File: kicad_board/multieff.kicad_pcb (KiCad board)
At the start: 2 copper layers, 120 x 108.8 mm, 86 parts, among them J1 Wha1, K1 HEADER_MALE_5X1, K2 HEADER_MALE_4X1, K3 easyC-SMD, K4 easyC-SMD, K5 HEADER_MALE_1X1, U1 ADS1115, U1 MCP23017_SO, U2 MCP23017_SO

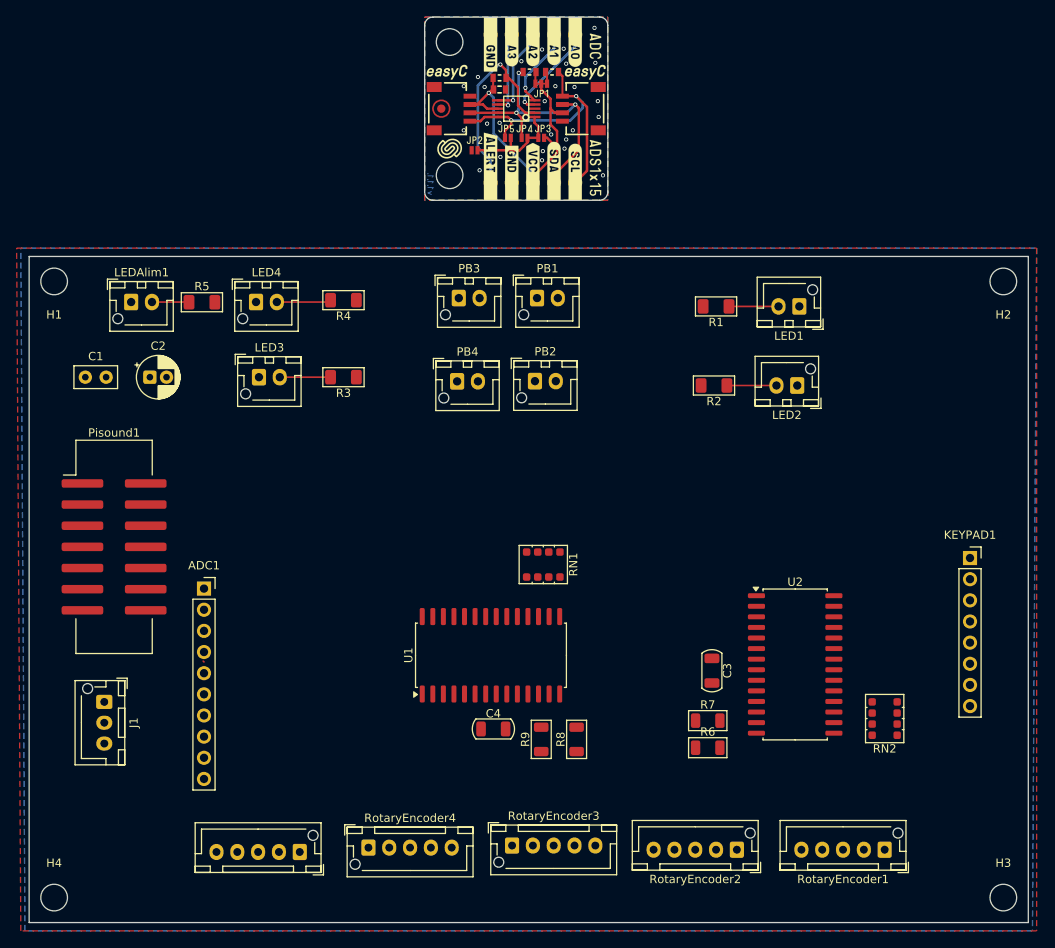
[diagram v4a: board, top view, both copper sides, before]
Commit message: First complete IC based version
Still miss some decoupling condensators.
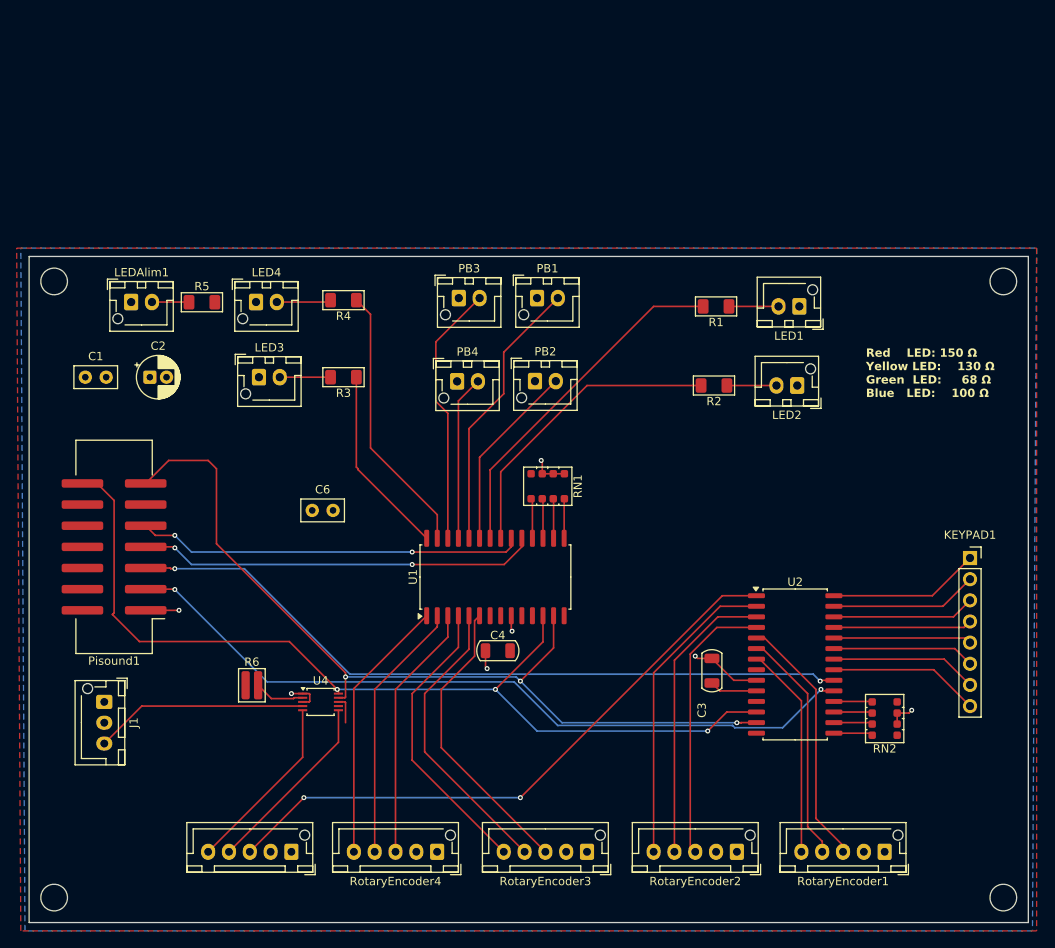
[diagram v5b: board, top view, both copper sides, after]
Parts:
- removed ? (x21): , buzzardLabel
- removed ADC1: Conn_01x10, Connector_PinSocket_2.54mm:PinSocket_1x10_P2.54mm_Vertical
- removed the C1 at (98.5, 11.9)
- removed FD1: FIDUCIAL, e-radionica.com footprinti:FIDUCIAL_23
- removed G***: LOGO, Soldered Graphics:Logo-Back-OSH-3.5mm
- removed G*** (x2): LOGO, Soldered Graphics:Logo-Front-easyC-5mm
- removed G***: LOGO, Soldered Graphics:Logo-Front-Soldered-3mm
- removed G***: LOGO, Soldered Graphics:Symbol-Front-Voltmeter
- removed the H1 at (92.5, 6.25)
- removed the H2 at (92.5, 22.2)
- removed JP1: SMD_JUMPER_3_PAD_TRACE, e-radionica.com footprinti:SMD_JUMPER_3_PAD_TRACE
- removed JP2: 0x48, e-radionica.com footprinti:SMD_JUMPER_CONNECTED
- removed JP3: 0x49, e-radionica.com footprinti:SMD_JUMPER
- removed JP4: 0x4A, e-radionica.com footprinti:SMD_JUMPER
- removed JP5: 0x4B, e-radionica.com footprinti:SMD_JUMPER
- removed K1: HEADER_MALE_5X1, e-radionica.com footprinti:HEADER_MALE_5X1
- removed K2: HEADER_MALE_4X1, e-radionica.com footprinti:HEADER_MALE_4X1
- removed K3, K4: easyC-SMD, e-radionica.com footprinti:easyC-connector
- removed K5: HEADER_MALE_1X1, e-radionica.com footprinti:HEADER_MALE_1X1
- removed the R1 at (98.5, 10.6)
- removed the R2 at (104.8, 9.85)
- removed the R3 at (102.1, 9.85)
- removed R7, R8, R9: 10k, PCM_Resistor_SMD_AKL:R_1206_3216Metric
- removed REF**: Logo-Front-SolderedFULL-13mm, Soldered Graphics:Logo-Back-SolderedFULL-13mm
- removed REF**: Version1.1.1., Soldered Graphics:Version1.1.1.
- removed REF**: Symbol-Front-I2C-ADDR-Field, Soldered Graphics:Symbol-Front-I2C-ADDR-Field
- removed the U1 at (100.5, 14.2)
- added C6: 1uF, Capacitor_THT:C_Disc_D5.0mm_W2.5mm_P2.50mm, F.Cu at (76.0, 62.5)
- added U4: ADS1115IDGS, Package_SO:TSSOP-10_3x3mm_P0.5mm, F.Cu at (77.0, 85.5)
- C3, C4: value 1uF -> 0.1uF
- R1: value 480 -> 150
- R2: value 480 -> 130
- R3: value 480 -> 68
- R4, R5: value 480 -> 100
- R6: footprint PCM_Resistor_SMD_AKL:R_1206_3216Metric -> PCM_Resistor_SMD_AKL:R_0612_1632Metric
- moved R6 55.3 mm to (68.8, 83.5)
- moved C4 9.42 mm to (98.3, 79.3)
- moved U1 9.42 mm to (98.0, 70.5)
- moved RN1 9.42 mm to (104.3, 59.6)
- moved RotaryEncoder3 9.03 mm to (109.0, 103.5), turned to 180 degrees
- moved RotaryEncoder4 8.27 mm to (91.0, 103.5), turned to 180 degrees
- moved Joystick1 1.00 mm to (73.5, 103.5)
- moved RotaryEncoder1 0.25 mm to (144.8, 103.5)
- moved RotaryEncoder2 0.25 mm to (127.0, 103.5)
- turned Pisound1 to 180 degrees
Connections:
- Pisound1 pad 11: unconnected-(Pisound1-Pin_11-Pad11) -> +3.3V
- R1 pad 2: Net-(U1-GPA4) -> Net-(U1-GPA1)
- R2 pad 2: Net-(U1-GPA6) -> Net-(U1-GPA0)
- R3 pad 1: Net-(U1-GPA0) -> Net-(U1-GPA7)
- R4 pad 1: Net-(U1-GPA1) -> Net-(U1-GPA6)
- R6 pad 2: /SDA -> Net-(U4-ALERT/RDY)
- U1 pad 1: Net-(RotaryEncoder4-Pin_3) -> Net-(RotaryEncoder4-Pin_5)
- U1 pad 23: Net-(PB3-Pin_2) -> Net-(PB2-Pin_2)
- U1 pad 24: Net-(PB4-Pin_2) -> Net-(PB1-Pin_2)
- U1 pad 25: Net-(U1-GPA4) -> Net-(PB4-Pin_2)
- U1 pad 26: Net-(PB1-Pin_2) -> Net-(PB3-Pin_2)
- U1 pad 28: Net-(PB2-Pin_2) -> Net-(U1-GPA7)
- U1 pad 3: Net-(RotaryEncoder4-Pin_5) -> Net-(RotaryEncoder4-Pin_3)
- U1 pad 4: Net-(RotaryEncoder3-Pin_3) -> Net-(RotaryEncoder3-Pin_5)
- U1 pad 6: Net-(RotaryEncoder3-Pin_5) -> Net-(RotaryEncoder3-Pin_3)
- U2 pad 5: Net-(RotaryEncoder1-Pin_5) -> Net-(RotaryEncoder1-Pin_3)
- U2 pad 7: Net-(RotaryEncoder1-Pin_3) -> Net-(RotaryEncoder1-Pin_5)
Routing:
- net /SCL: track 0.00 -> 114.3 mm, vias 0 -> 3
- net /SDA: track 0.00 -> 105.9 mm, vias 0 -> 3
- net Net-(Pisound1-Pin_3): track 0.00 -> 91.7 mm, vias 0 -> 2
- net Net-(Pisound1-Pin_5): track 0.00 -> 88.3 mm, vias 0 -> 2
- net Net-(Joystick1-Pin_3): track 0.00 -> 73.7 mm, vias 0 -> 2
- net Net-(Pisound1-Pin_7): track 0.00 -> 48.0 mm, vias 0 -> 2
- net Net-(Pisound1-Pin_9): track 0.00 -> 46.5 mm, vias 0 -> 2
- net Net-(U1-GPA1): track 0.00 -> 41.9 mm
- net VCC: track 41.0 -> 0.00 mm, vias 1 -> 0
- net Net-(RotaryEncoder2-Pin_5): track 0.00 -> 37.2 mm
- net Net-(U1-GPA0): track 0.00 -> 36.3 mm
- net SCL: track 35.8 -> 0.00 mm, vias 2 -> 0
- net Net-(RotaryEncoder3-Pin_4): track 0.00 -> 35.5 mm
- net Net-(RotaryEncoder3-Pin_3): track 0.00 -> 35.4 mm
- net Net-(RotaryEncoder3-Pin_5): track 0.00 -> 35.2 mm
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- removed copper zone on F.Cu, net GND
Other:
- board size 120 x 108.8 mm -> 120 x 80 mm
- board text added: "Kleag's Effects Board"
- board text added: "Licensed under CERN-OHL-W v2"
- board text added: "Red LED: 150 Ω Yellow LED: 130 Ω Green LED: 68 Ω Blue LED: 100 Ω"
- board text added: "https://github.com/kleag/kleagmfx"
- board text removed: "Joystick"

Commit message: Chips decoupling complete
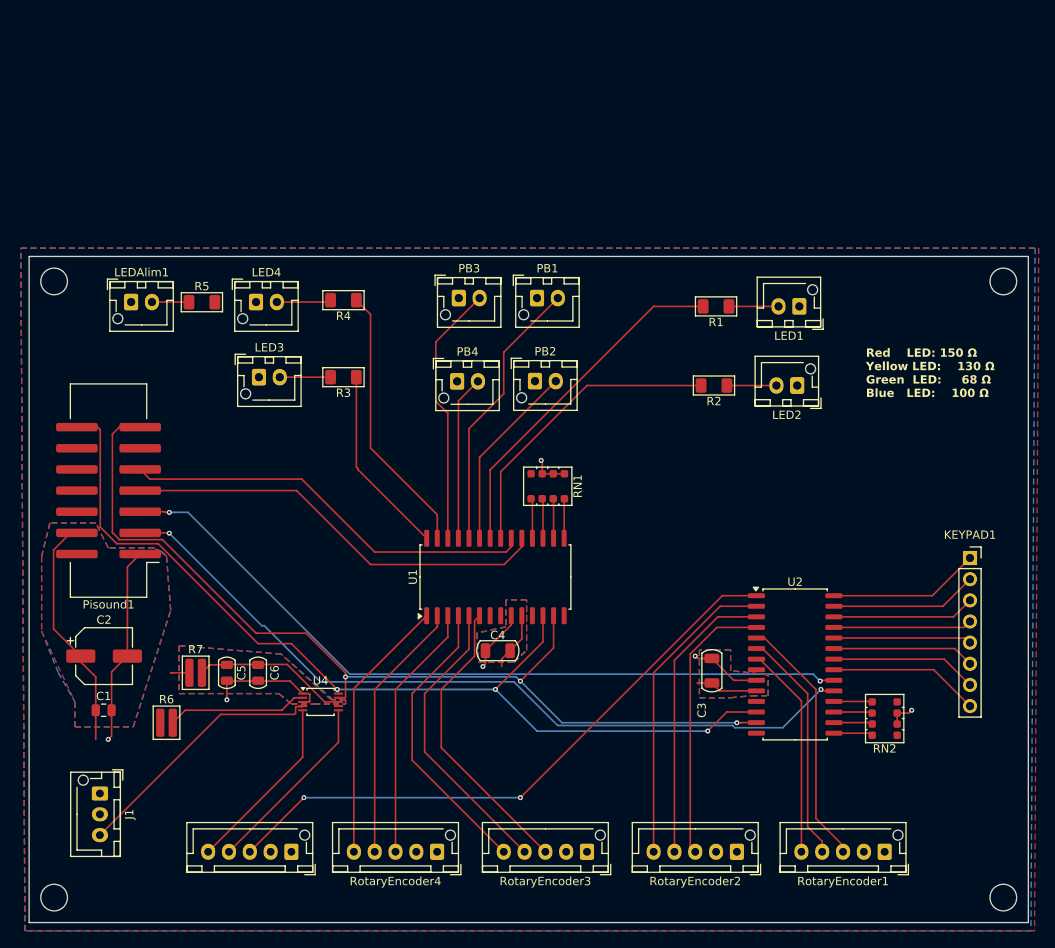
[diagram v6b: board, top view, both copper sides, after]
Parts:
- added C5: 0.1uF, PCM_Capacitor_SMD_AKL:C_0805_2012Metric, F.Cu at (65.8, 82.0)
- added R7: 10, PCM_Resistor_SMD_AKL:R_0612_1632Metric, F.Cu at (62.0, 82.0)
- C1: footprint Capacitor_THT:C_Disc_D5.0mm_W2.5mm_P2.50mm -> Capacitor_SMD:C_0805_2012Metric
- C2: footprint Capacitor_THT:CP_Radial_D5.0mm_P2.00mm -> Capacitor_SMD:CP_Elec_6.3x5.4
- C6: value 1uF -> 10uF; footprint Capacitor_THT:C_Disc_D5.0mm_W2.5mm_P2.50mm -> PCM_Capacitor_SMD_AKL:C_0805_2012Metric
- moved C1 40.1 mm to (51.0, 86.5)
- moved C2 33.9 mm to (51.0, 80.0)
- moved C6 20.6 mm to (69.5, 82.0), turned to -90 degrees
- moved R6 11.2 mm to (58.5, 88.0)
- moved J1 11.0 mm to (50.5, 96.5)
- moved Pisound1 6.79 mm to (51.5, 60.1)
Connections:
- C6 pad 1: +3.3V -> Net-(U4-VDD)
- Pisound1 pad 11: +3.3V -> unconnected-(Pisound1-Pin_11-Pad11)
- U4 pad 8: +3.3V -> Net-(U4-VDD)
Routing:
- net +3.3V: track 9.08 -> 45.6 mm
- net GND: track 28.2 -> 62.1 mm, vias 7 -> 6
- net Net-(U4-VDD): track 0.00 -> 18.7 mm
- net Net-(U4-ALERT/RDY): track 6.05 -> 16.8 mm
- net /SDA: track 105.9 -> 115.4 mm
- net Net-(J1-Pin_3): track 25.7 -> 31.2 mm
- net Net-(Pisound1-Pin_5): track 88.3 -> 91.8 mm
- net Net-(Pisound1-Pin_7): track 48.0 -> 51.4 mm, vias 2 -> 0
- net Net-(Pisound1-Pin_3): track 91.7 -> 95.2 mm
- net Net-(Pisound1-Pin_9): track 46.5 -> 50.0 mm, vias 2 -> 0
- net /SCL: track 114.3 -> 116.3 mm

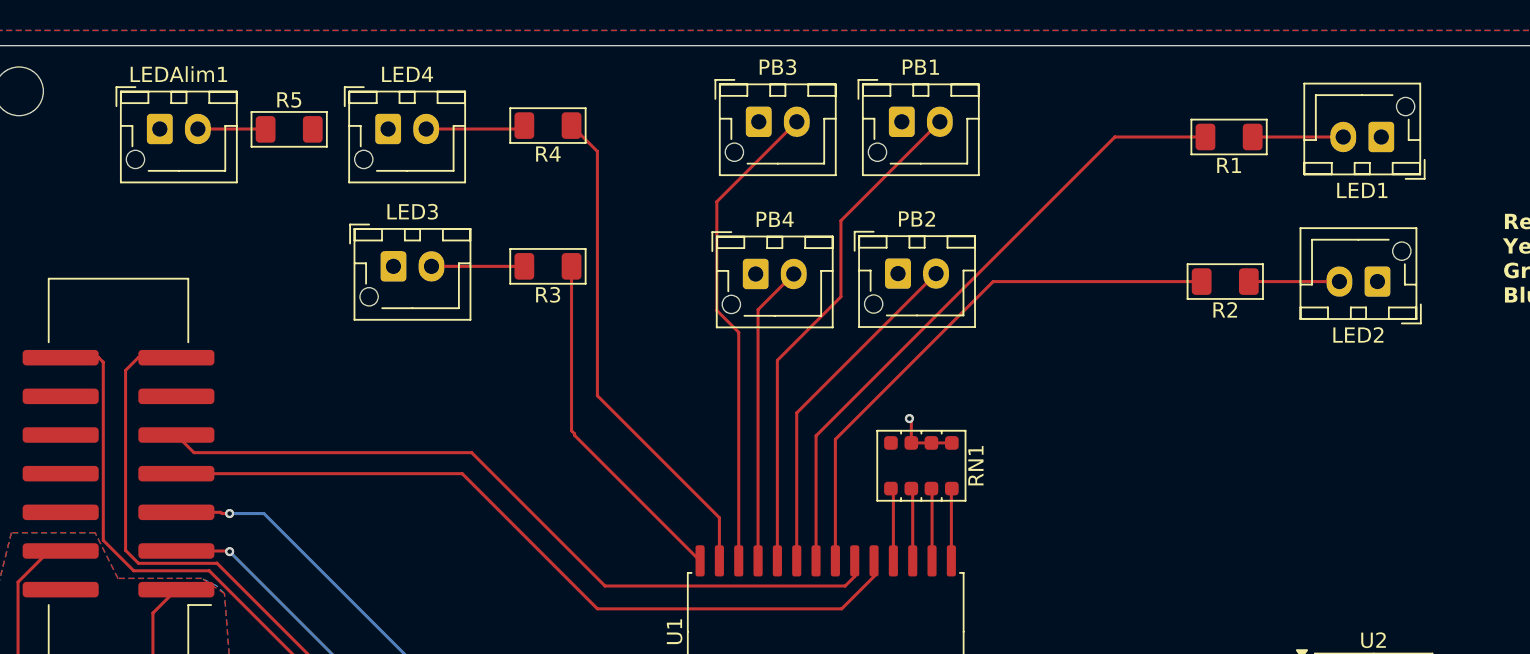
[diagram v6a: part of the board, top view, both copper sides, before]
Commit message: Add decoupling capacitors to LEDs
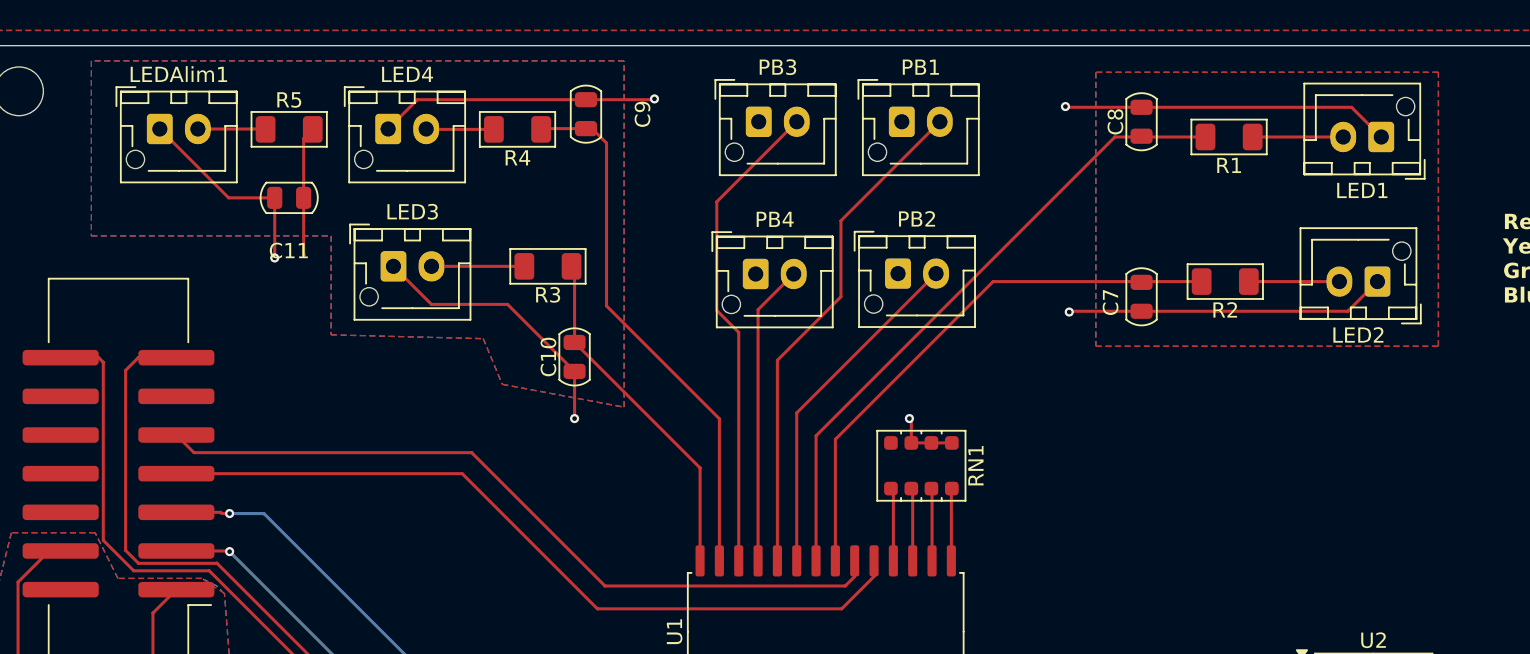
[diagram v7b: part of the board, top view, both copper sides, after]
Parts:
- added C10: 47uF, PCM_Capacitor_SMD_AKL:C_0805_2012Metric, F.Cu at (81.5, 52.5)
- added C11: 47uF, PCM_Capacitor_SMD_AKL:C_0805_2012Metric, F.Cu at (62.8, 42.0)
- added C7: 47uF, PCM_Capacitor_SMD_AKL:C_0805_2012Metric, F.Cu at (118.8, 48.5)
- added C8: 47uF, PCM_Capacitor_SMD_AKL:C_0805_2012Metric, F.Cu at (118.8, 37.0)
- added C9: 47uF, PCM_Capacitor_SMD_AKL:C_0805_2012Metric, F.Cu at (82.2, 36.5)
- moved R4 2.02 mm to (77.8, 37.5)
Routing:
- net GND: track 62.1 -> 154.4 mm, vias 6 -> 11
- net +3.3V: track 45.6 -> 54.2 mm
- net Net-(LED4-Pin_2): track 6.54 -> 4.46 mm
- net Net-(U1-GPA6): track 32.6 -> 34.7 mm

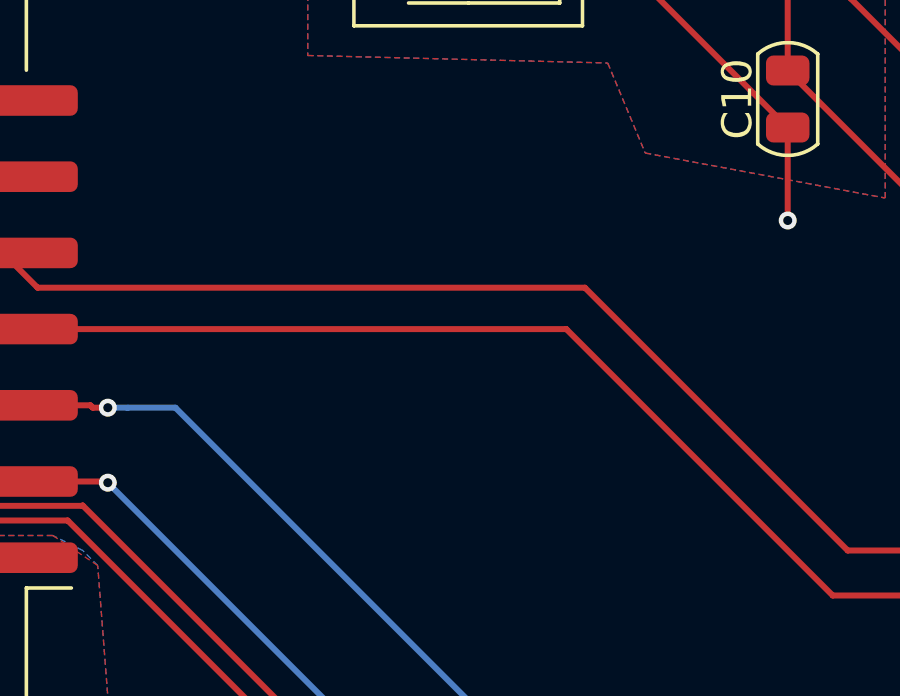
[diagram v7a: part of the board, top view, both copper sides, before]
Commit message: Add missing screen alim connector
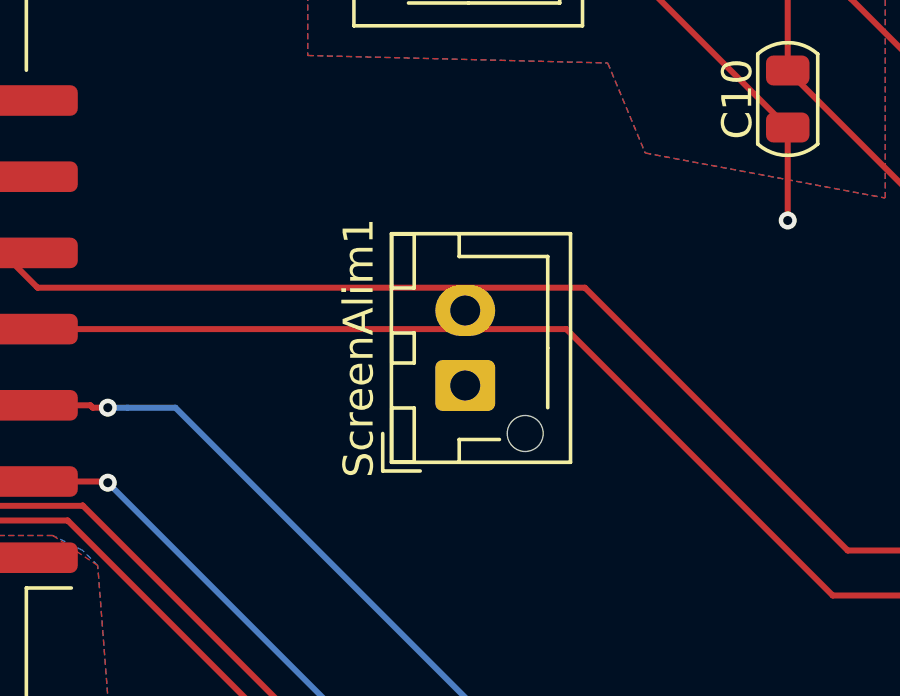
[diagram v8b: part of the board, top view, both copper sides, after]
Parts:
- added ScreenAlim1: Conn_01x02, Connector_JST:JST_XH_B2B-XH-AM_1x02_P2.50mm_Vertical, F.Cu at (70.8, 62.0)
